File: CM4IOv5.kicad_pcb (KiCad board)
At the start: 4 copper layers, 115.1 x 61 mm, 115 parts, among them J1 Conn_01x02, J10 HDMI_C_1.4, J11 HDMI_C_1.4, J13 Conn_01x03, J14 Conn_01x03, J15 Audio OUT, J16 Micro_SD_Card_Det, J17 THD-20-R, J2 Bus_M.2_Socket_B, J3 USB_OTG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

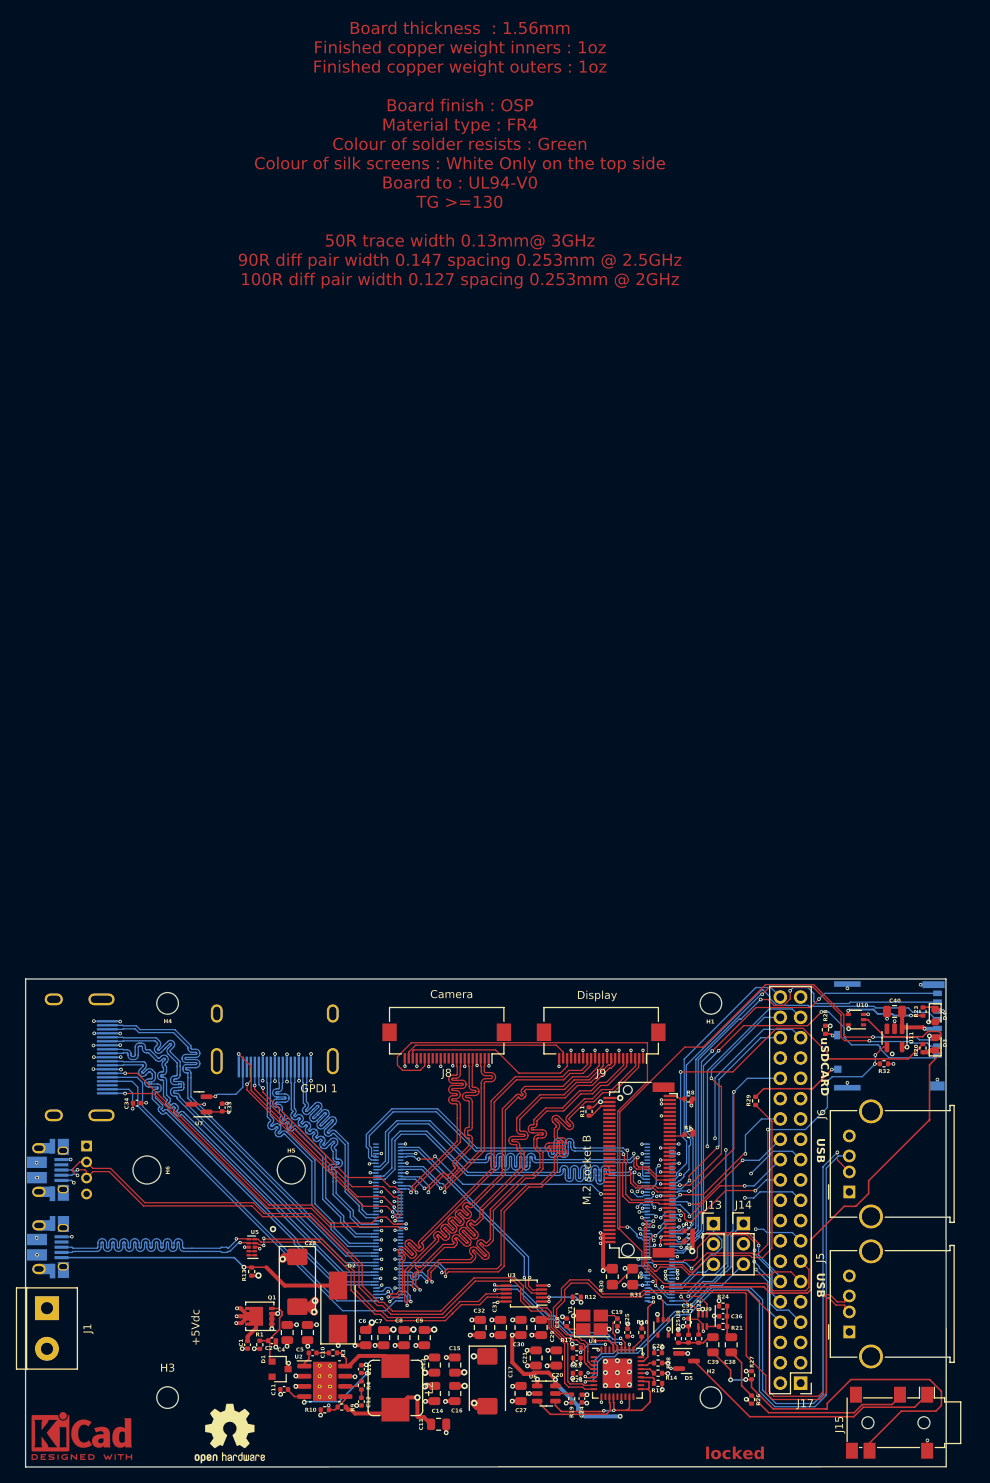
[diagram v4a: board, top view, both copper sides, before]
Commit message: Fixing errors, fixing most warnings
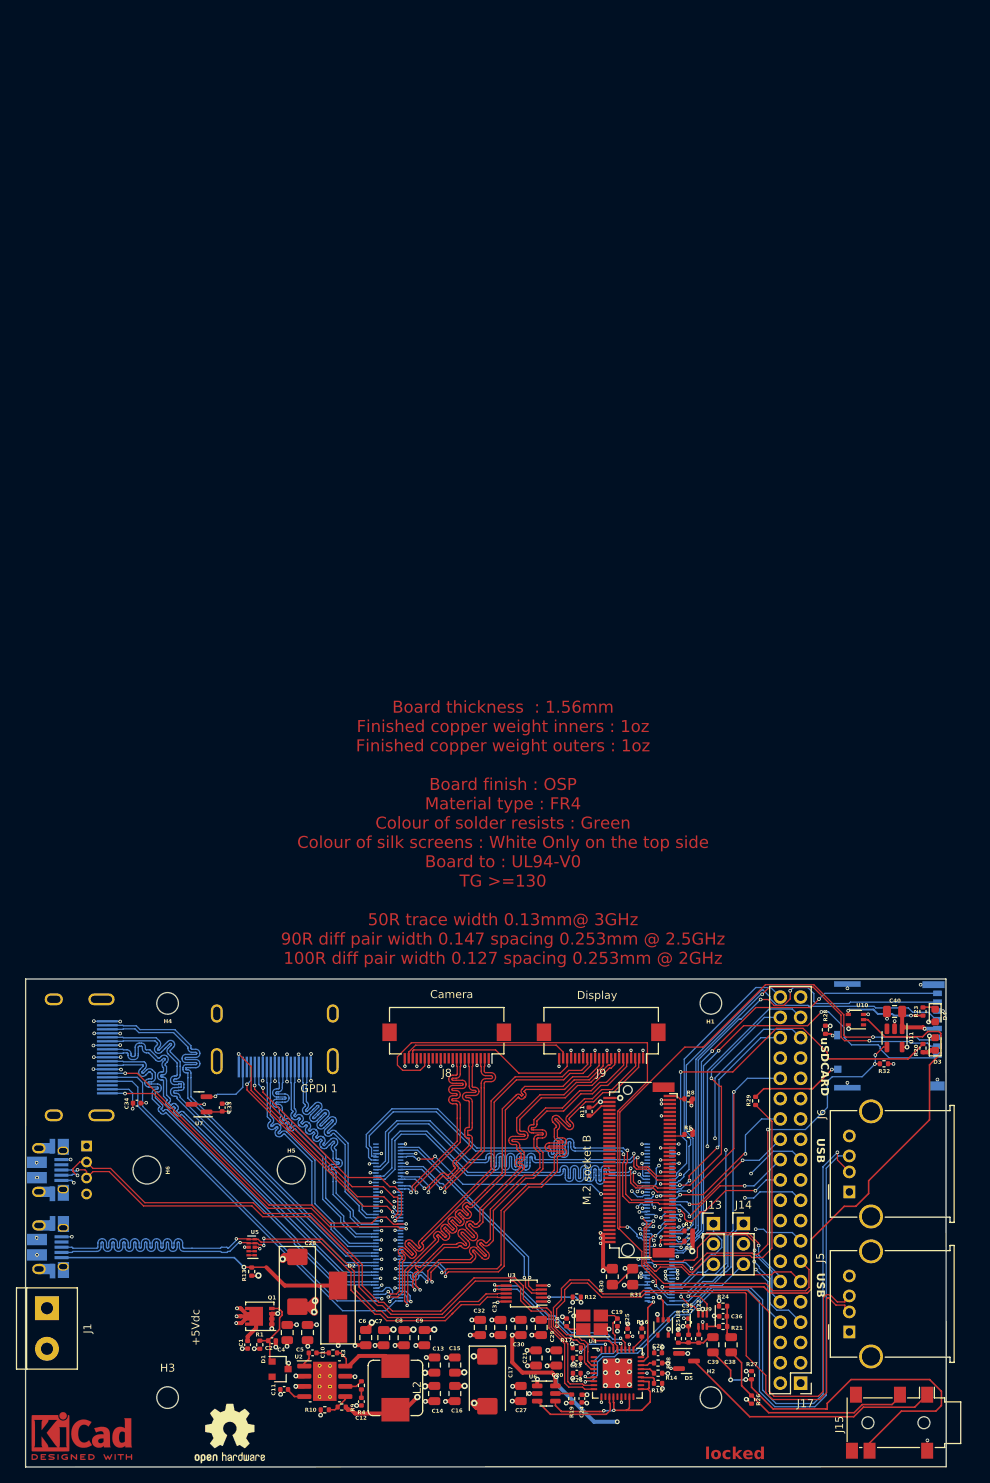
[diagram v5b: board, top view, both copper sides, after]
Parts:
- removed the C11 at (138.8, 127.8)
- removed the C13 at (148.4, 134.7)
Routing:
- net /+3.3v: track 322.7 -> 370.4 mm, vias 37 -> 36
- net Net-(U2-SS): track 13.4 -> 2.45 mm, vias 2 -> 0
- net /+3.3vSSD: track 101.5 -> 96.9 mm
- net /CM4_GPIO (GPIO, SDCARD)/+1.8v: track 5.12 -> 8.88 mm, vias 3 -> 2
- net GND: track 175.4 -> 173.6 mm, vias 180 -> 178
- net /CM4_GPIO (GPIO, SDCARD)/AUDIO_L: track 27.9 -> 27.0 mm
- net /+5v: track 213.6 -> 213.0 mm, vias 24 -> 23
- net Net-(U2-FB): track 3.50 -> 2.94 mm, vias 1 -> 0
- net /USB2-HUB/VBUS: track 162.9 -> 163.5 mm, vias 9 -> 8

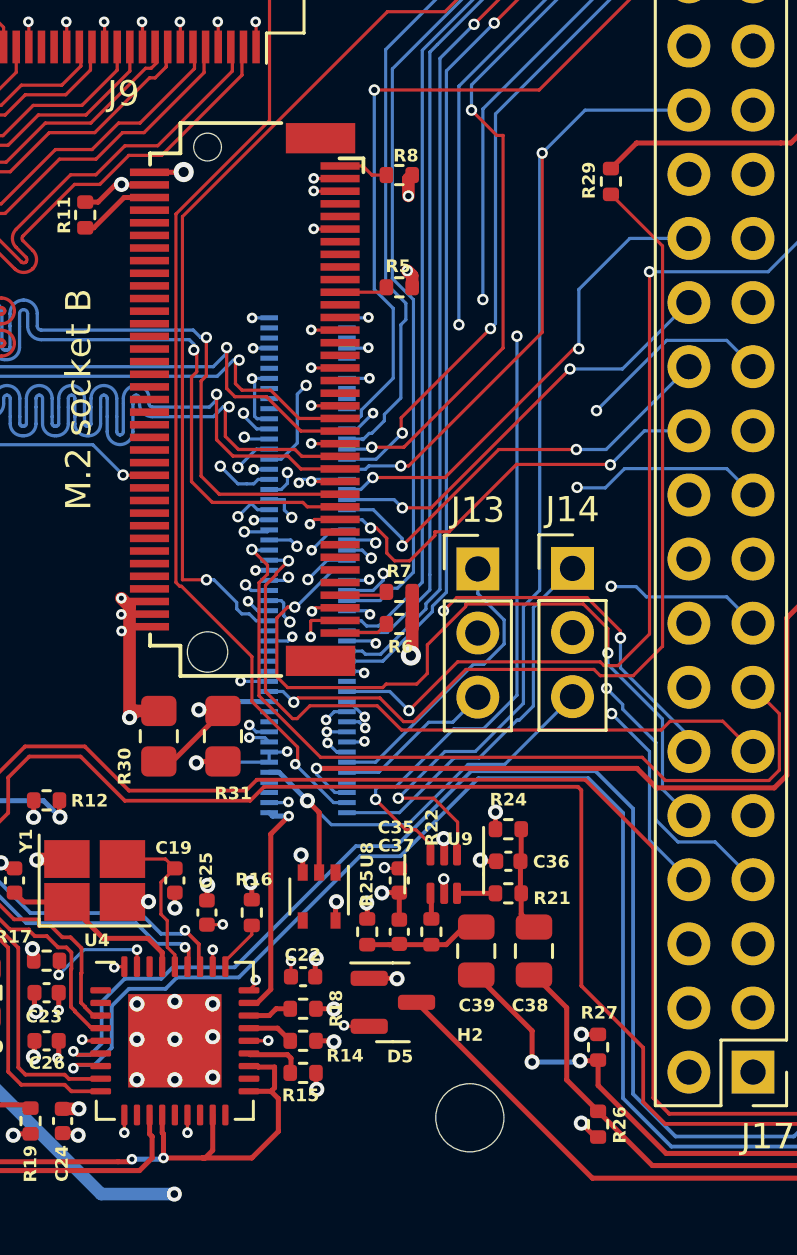
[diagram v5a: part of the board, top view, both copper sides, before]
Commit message: Adding GlobalENable, and RpiBoot
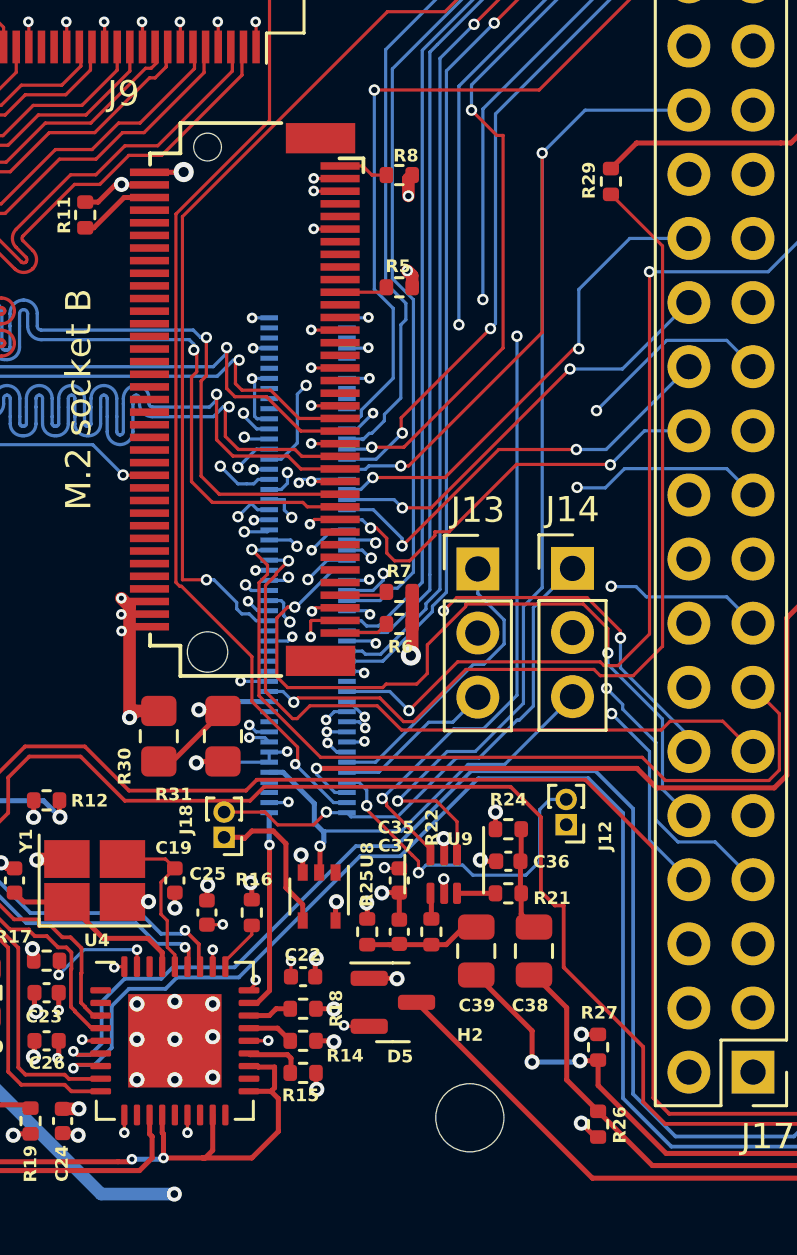
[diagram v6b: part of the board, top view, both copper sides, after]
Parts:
- added J12: nRpiBoot, Connector_PinHeader_1.00mm:PinHeader_1x02_P1.00mm_Vertical, F.Cu at (186.3, 119.7)
- added J18: GLOBAL_EN, Connector_PinHeader_1.00mm:PinHeader_1x02_P1.00mm_Vertical, F.Cu at (172.8, 120.2)
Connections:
- U8 pad 4: unconnected-(U8-Pad4) -> Net-(J18-Pin_1)
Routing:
- net /CM4_GPIO (GPIO, SDCARD)/nRPIBOOT: track 0.00 -> 13.6 mm, vias 0 -> 2
- net Net-(J18-Pin_1): track 0.00 -> 6.12 mm
- net /CM4_GPIO (GPIO, SDCARD)/GLOBAL_EN: track 15.2 -> 20.7 mm, vias 0 -> 1
- net /USB2-HUB/HD2_N: track 74.3 -> 72.9 mm
- net /nEXTRST: track 9.07 -> 8.07 mm
- net /CM4_GPIO (GPIO, SDCARD)/GPIO13: track 64.5 -> 63.6 mm
- net /CM4_GPIO (GPIO, SDCARD)/RUN_PG: track 18.0 -> 17.3 mm

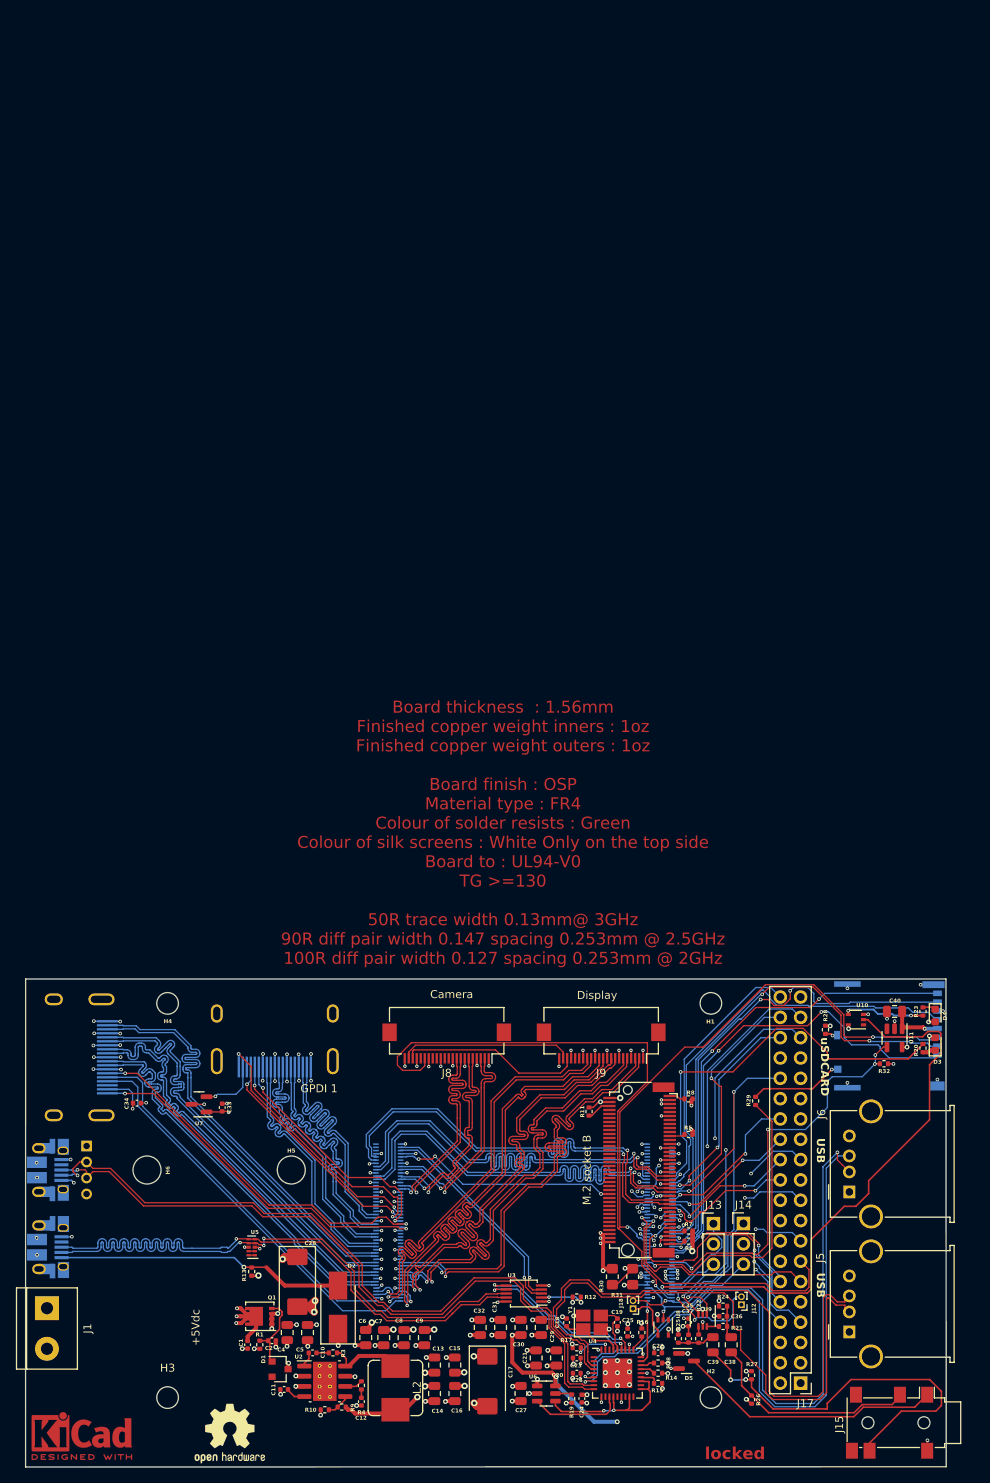
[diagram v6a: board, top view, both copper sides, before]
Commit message: Adding audio connector - fixing USB, adding logos
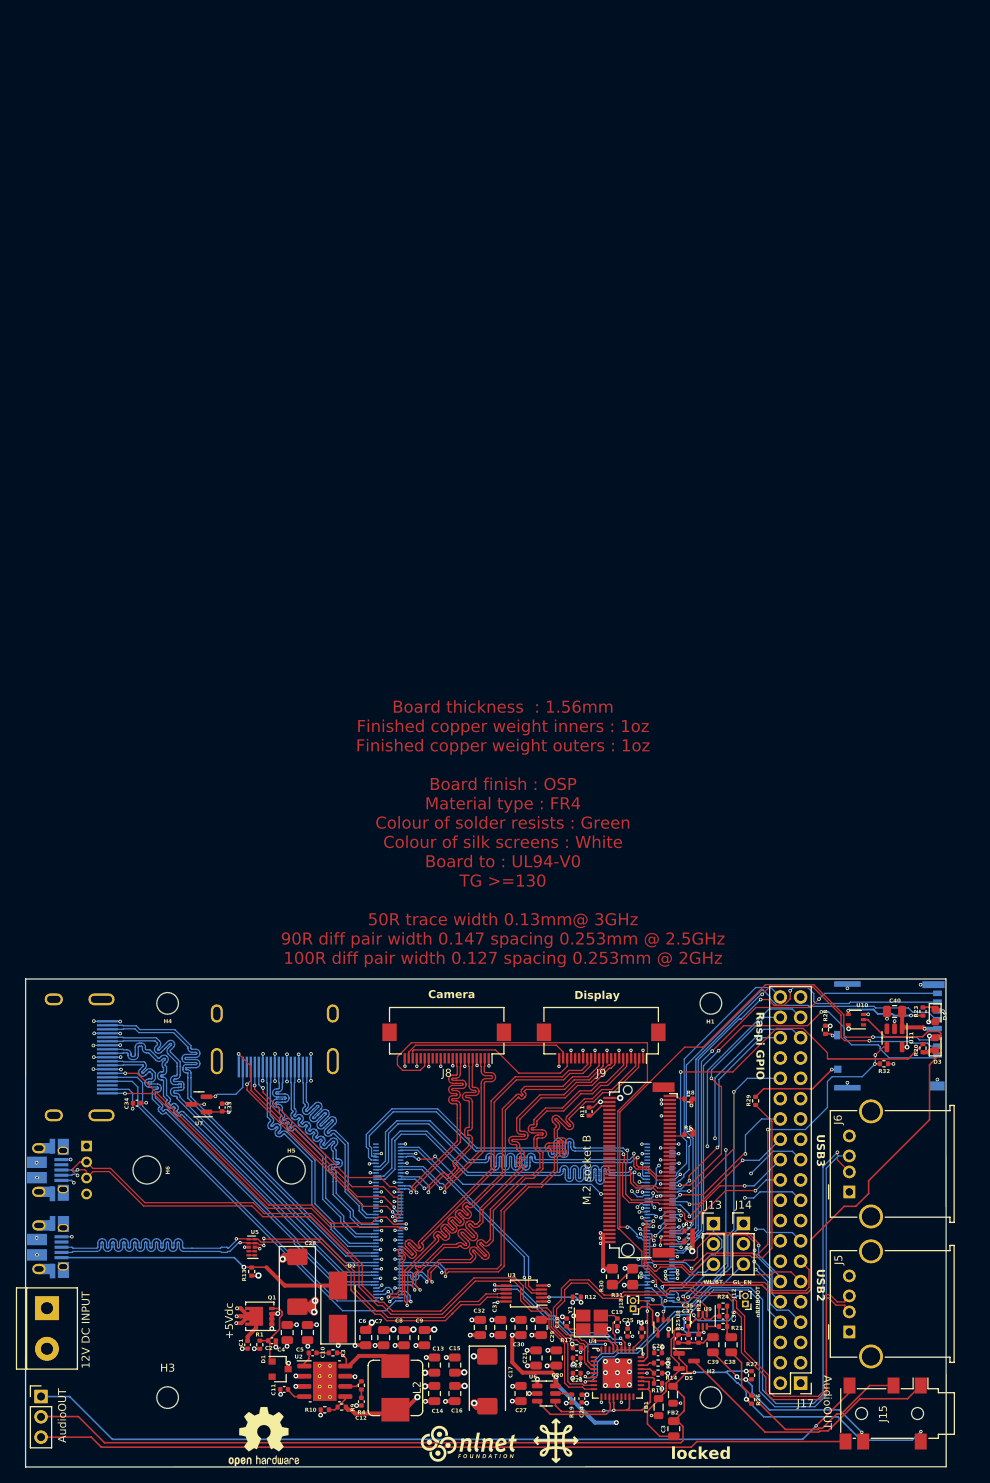
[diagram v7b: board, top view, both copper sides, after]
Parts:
- removed the REF** at (103.8, 136.1)
- added C3: 10u, Capacitor_SMD:C_0805_2012Metric, F.Cu at (177.8, 135.2)
- added FB1: FerriteBead, Inductor_SMD:L_0805_2012Metric, F.Cu at (175.9, 132.5)
- added FB2: FerriteBead, Inductor_SMD:L_0805_2012Metric, F.Cu at (177.8, 130.9)
- added G***: LOGO, CM4IO:balthazar-logo, F.Cu at (163.1, 136.7)
- added G***: LOGO, CM4IO:nlnet-logo, F.Cu at (152.2, 137.1)
- added G***: LOGO, CM4IO:balthazar-logo, B.Cu at (114.2, 114.3)
- added G***: LOGO, CM4IO:nlnet-logo, B.Cu at (114.8, 108.7)
- added J19: AudioAMP, Connector_PinHeader_2.54mm:PinHeader_1x03_P2.54mm_Vertical, F.Cu at (98.8, 131.2)
- added REF**: OSHW-Logo2_9.8x8mm_SilkScreen, Symbol:OSHW-Logo2_9.8x8mm_SilkScreen, B.Cu at (114.2, 121.9)
- J15: value Audio OUT -> AudioOUT
- moved REF** 4.28 mm to (126.6, 136.2)
- moved J15 1.40 mm to (204.0, 133.3)
- moved J12 0.51 mm to (186.8, 119.6)
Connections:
- C35 pad 1: /+3.3v -> Net-(D5-A)
- C35 pad 2: GND -> Net-(D5-K)
- C36 pad 2: GND -> Net-(D5-K)
- C37 pad 2: GND -> Net-(D5-K)
- D5 pad 1: GND -> Net-(D5-K)
- D5 pad 2: /+3.3v -> Net-(D5-A)
- J15 pad 2: GND -> Net-(D5-K)
- J15 pad 5: (no net) -> Net-(J19-Pin_3)
- J15 pad 6: (no net) -> Net-(J19-Pin_1)
- R24 pad 1: GND -> Net-(D5-K)
- R25 pad 1: GND -> Net-(D5-K)
- R26 pad 1: GND -> Net-(D5-K)
- R27 pad 1: GND -> Net-(D5-K)
- U9 pad 2: GND -> Net-(D5-K)
- U9 pad 5: /+3.3v -> Net-(D5-A)
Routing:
- net Net-(D5-K): track 0.00 -> 146.6 mm, vias 0 -> 4
- net Net-(J19-Pin_1): track 0.00 -> 106.6 mm, vias 0 -> 1
- net Net-(J19-Pin_3): track 0.00 -> 101.4 mm
- net Net-(D5-A): track 0.00 -> 24.6 mm, vias 0 -> 3
- net /CM4_GPIO (GPIO, SDCARD)/AUDIO_R: track 49.1 -> 25.2 mm, vias 2 -> 3
- net /+3.3v: track 370.6 -> 362.2 mm, vias 36 -> 34
- net GND: track 173.6 -> 166.3 mm, vias 178 -> 170
- net /USB2-HUB/VBUS: track 163.5 -> 166.5 mm
- net Net-(D5-K)_1: track 33.2 -> 34.4 mm
- net /CM4_GPIO (GPIO, SDCARD)/AUDIO_L: track 27.0 -> 28.2 mm
- net /USB2-HUB/HD2_P: track 75.3 -> 74.1 mm
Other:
- board text added: "+"
- board text added: "-"
- board text added: "12V DC INPUT"
- board text added: "Board thickness : 1.56mm Finished copper weight inners : 1oz Finished copper weight outers : 1oz Board finish : OSP Material type : FR4 Colour of solder resists : Green Colour of silk screens : White Board to : UL94-V0 TG >=130 50R trace width 0.13mm@ 3GHz 90R diff pair width 0.147 spacing 0.253mm @ 2.5GHz 100R diff pair width 0.127 spacing 0.253mm @ 2GHz"
- board text added: "GL_EN"
- board text added: "GPDI0"
- board text added: "GPDI1"
- board text added: "Raspi GPIO"
- board text added: "USB1"
- board text added: "USB2"
- board text added: "USB3"
- board text added: "USB4"
- board text added: "WL/BT"
- board text added: "nRPIBOOT"
- board text removed: "Board thickness : 1.56mm Finished copper weight inners : 1oz Finished copper weight outers : 1oz Board finish : OSP Material type : FR4 Colour of solder resists : Green Colour of silk screens : White Only on the top side Board to : UL94-V0 TG >=130 50R trace width 0.13mm@ 3GHz 90R diff pair width 0.147 spacing 0.253mm @ 2.5GHz 100R diff pair width 0.127 spacing 0.253mm @ 2GHz"
- board text removed: "GPDI 1"
- board text removed: "USB"
